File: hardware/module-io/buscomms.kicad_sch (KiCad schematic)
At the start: 10 parts, among them J6 RJ45_LED_Shielded, J7 RJ45_LED_Shielded, U1 MAX485E, U2 MAX485E

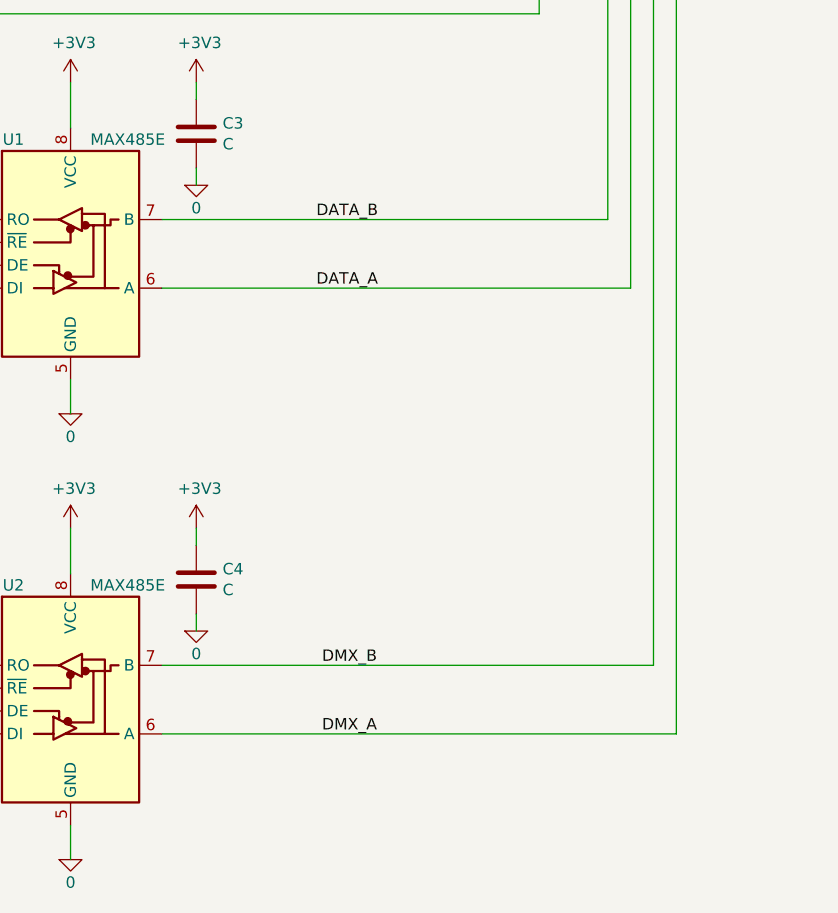
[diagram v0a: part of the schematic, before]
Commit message: feat: add protection to bus conns io
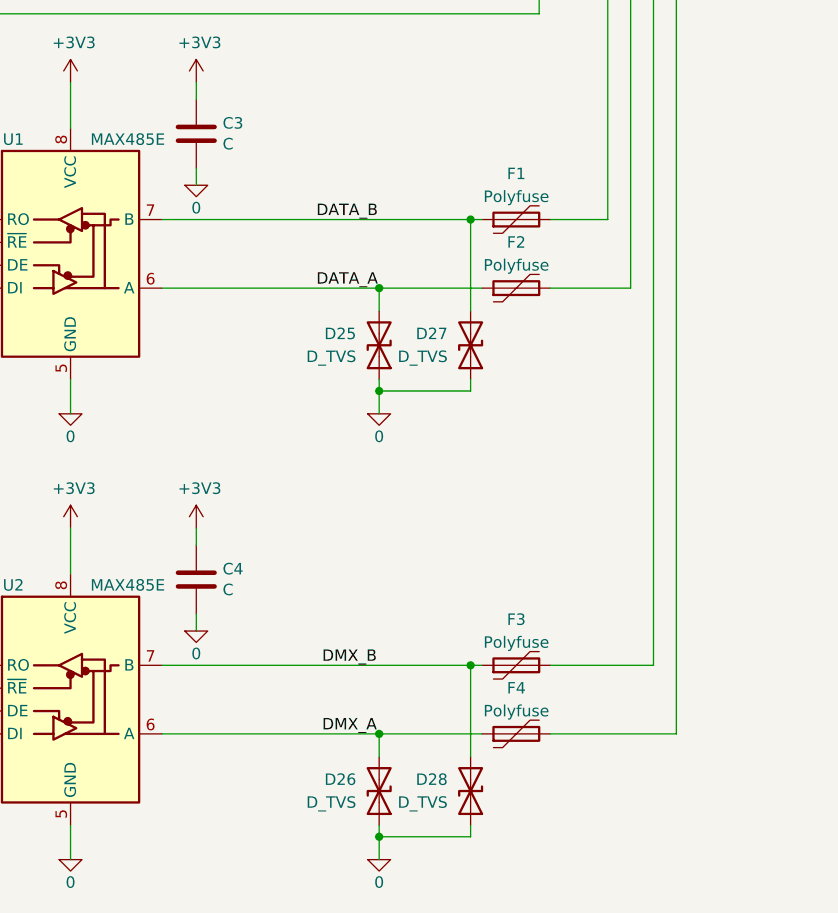
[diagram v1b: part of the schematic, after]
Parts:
- added D25, D26, D27, D28: D_TVS, Diode_SMD:D_SMB_Handsoldering, symbol Device:D_TVS
- added F1, F2, F3, F4: Polyfuse, Fuse:Fuse_1812_4532Metric_Pad1.30x3.40mm_HandSolder, symbol Device:Polyfuse
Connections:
- net 0: now also D25.1 (A1), D26.1 (A1), D27.1 (A1), D28.1 (A1)
- net DATA_A: now also D25.2 (A2), F2.1; no longer J6.5, J7.5
- net DATA_B: now also D27.2 (A2), F1.1; no longer J6.6, J7.6
- net DMX_A: now also D26.2 (A2), F4.1; no longer J6.7, J7.7
- net DMX_B: now also D28.2 (A2), F3.1; no longer J6.8, J7.8
- new net: F2.2, J6.5, J7.5
- new net: F1.2, J6.6, J7.6
- new net: F4.2, J6.7, J7.7
- new net: F3.2, J6.8, J7.8
